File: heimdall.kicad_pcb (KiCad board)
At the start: 2 copper layers, 20 x 32 mm, 20 parts, among them P1 CONN, Q1 FDN304P, U1 ESP-01, U2 TLP222A, U3 TPS62177

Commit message: Various shuffling
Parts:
- R1: footprint Resistors_SMD:R_1206 -> Resistors_SMD:R_0603
- moved R2 8.41 mm to (102.2, 101.4)
- moved Q1 8.40 mm to (110.8, 101.3)
- moved R3 7.56 mm to (107.0, 103.1), turned to 0 degrees
- moved F1 5.67 mm to (109.1, 91.3), turned to 0 degrees
- moved C2 4.12 mm to (112.1, 102.0)
- moved C1 3.00 mm to (105.4, 95.3)
- moved L1 3.00 mm to (105.0, 98.5)
- moved U3 3.00 mm to (104.0, 94.4)
- moved C6 3.00 mm to (104.3, 93.1)
- moved D1 2.16 mm to (103.3, 87.0)
- moved R1 1.53 mm to (114.0, 102.7)
- moved C3 1.27 mm to (103.7, 107.2)
- moved C4 0.06 mm to (116.4, 108.4)
- moved C5 0.06 mm to (118.0, 108.4)
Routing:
- net +3V3: track 33.4 -> 26.6 mm
- net /SW0: track 11.1 -> 4.32 mm
- net /VCC: track 16.5 -> 11.5 mm
- net /PG: track 16.8 -> 11.8 mm
- net /PWROUT: track 4.48 -> 8.79 mm
- net /RELAY_TRIGGER: track 3.51 -> 4.77 mm
- net /SW0_IN: track 7.52 -> 8.53 mm
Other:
- board text added: "SW"
- board text removed: "SW0"
- board text removed: "SW1"

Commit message: More faffing
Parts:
- moved F2 3.14 mm to (117.2, 102.6)
- moved F1 2.05 mm to (110.9, 92.3), turned to 270 degrees
- moved C5 1.98 mm to (117.1, 106.6), turned to 0 degrees
- moved Q1 1.84 mm to (109.0, 101.3)
- moved R3 1.84 mm to (105.2, 103.1)
- moved C2 1.77 mm to (110.4, 102.4)
- moved C4 1.01 mm to (117.1, 109.2), turned to 0 degrees
- moved R1 0.97 mm to (113.1, 102.6)
- moved U2 0.25 mm to (114.6, 98.8)
- turned D3 to 180 degrees
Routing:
- net GND: track 26.5 -> 29.1 mm, vias 4 -> 5
- net Net-(C4-Pad1): track 14.0 -> 16.2 mm
- net /PG: track 11.8 -> 10.0 mm
- net +3V3: track 26.6 -> 25.0 mm
- net /PWROUT: track 8.79 -> 8.15 mm
- net /SW0_IN: track 8.53 -> 9.09 mm

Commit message: PMOS NMOS fun
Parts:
- Q1: value FDN304P -> FDN337N
- moved Q1 2.60 mm to (107.1, 103.1), turned to 0 degrees
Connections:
- Q1 pad 2: /PWROUT -> +3V3
- Q1 pad 3: +3V3 -> /PWROUT
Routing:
- net /PWROUT: track 8.15 -> 7.00 mm
- net +3V3: track 25.0 -> 25.8 mm
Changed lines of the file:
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@@
     (thickness 1.6)
     (drawings 15)
-    (tracks 136)
+    (tracks 135)
     (zones 0)
     (modules 20)
@@
   )
   (setup
-    (last_trace_width 0.5)
+    (last_trace_width 0.25)
     (user_trace_width 0.1)
     (user_trace_width 0.2)
@@
   )
   (module Housings_SSOT:SuperSOT-3 (layer F.Cu)
-    (at 108.966 101.2825 180)
-    (fp_text reference Q1 (at 1 1.1 180) (layer F.SilkS) hide
-      (effects (font (size 0.8 0.8) (thickness 0.15)))
-    )
-    (fp_text value FDN304P (at 1 -3.35 180) (layer F.Fab) hide
+    (at 107.1245 103.124)
+    (fp_text reference Q1 (at 1 1.1) (layer F.SilkS) hide
+      (effects (font (size 0.8 0.8) (thickness 0.15)))
+    )
+    (fp_text value FDN337N (at 1 -3.35) (layer F.Fab) hide
       (effects (font (size 0.8 0.8) (thickness 0.15)))
     )
@@
     (fp_line (start -0.51 -1.845) (end 2.41 -1.845) (layer F.SilkS) (width 0.15))
     (fp_line (start -0.51 -0.445) (end 2.41 -0.445) (layer F.SilkS) (width 0.15))
-    (pad 2 smd rect (at 0.95 -2.29 180) (size 0.76 0.76) (layers F.Cu F.Paste F.Mask)
+    (pad 2 smd rect (at 0.95 -2.29) (size 0.76 0.76) (layers F.Cu F.Paste F.Mask)
+      (net 2 +3V3))
+    (pad 3 smd rect (at 1.9 0) (size 0.76 0.76) (layers F.Cu F.Paste F.Mask)
       (net 9 /PWROUT))
-    (pad 3 smd rect (at 1.9 0 180) (size 0.76 0.76) (layers F.Cu F.Paste F.Mask)
-      (net 2 +3V3))
-    (pad 1 smd rect (at 0 0 180) (size 0.76 0.76) (layers F.Cu F.Paste F.Mask)
+    (pad 1 smd rect (at 0 0) (size 0.76 0.76) (layers F.Cu F.Paste F.Mask)
       (net 10 "Net-(C2-Pad2)"))
     (model ${KISYS3DMOD}/TO_SOT_Packages_SMD.3dshapes/SOT-23.wrl
@@
   (segment (start 106.96702 88.138) (end 107.643 88.81398) (width 0.5) (layer F.Cu) (net 1))
   (segment (start 107.482 87.62302) (end 106.96702 88.138) (width 0.5) (layer F.Cu) (net 1) (status 30))
-  (segment (start 106.553 96.03175) (end 107.066 96.54475) (width 0.25) (layer F.Cu) (net 2))
-  (segment (start 107.066 96.54475) (end 107.066 101.2825) (width 0.25) (layer F.Cu) (net 2))
-  (segment (start 102.1715 100.6595) (end 106.443 100.6595) (width 0.25) (layer F.Cu) (net 2))
-  (segment (start 106.443 100.6595) (end 107.066 101.2825) (width 0.25) (layer F.Cu) (net 2))
+  (segment (start 106.553 96.03175) (end 108.0745 97.55325) (width 0.25) (layer F.Cu) (net 2))
+  (segment (start 108.0745 97.55325) (end 108.0745 100.834) (width 0.25) (layer F.Cu) (net 2) (status 800000))
+  (segment (start 102.1715 100.6595) (end 107.9 100.6595) (width 0.25) (layer F.Cu) (net 2) (status C00000))
+  (segment (start 107.9 100.6595) (end 108.0745 100.834) (width 0.25) (layer F.Cu) (net 2) (status C00000))
   (segment (start 101.473 98.425) (end 101.473 100.5205) (width 0.25) (layer F.Cu) (net 2))
   (segment (start 103.04475 96.29275) (end 103.04475 96.85325) (width 0.25) (layer F.Cu) (net 2))
@@
   (segment (start 104.1908 96.29275) (end 104.04475 96.29275) (width 0.25) (layer F.Cu) (net 2))
   (segment (start 106.09725 98.45675) (end 106.09725 96.75075) (width 0.25) (layer F.Cu) (net 2))
-  (segment (start 110.96498 88.138) (end 110.871 88.23198) (width 0.5) (layer F.Cu) (net 3) (status C00000))
-  (segment (start 110.871 88.23198) (end 110.871 90.879) (width 0.5) (layer F.Cu) (net 3) (status C00000))
+  (segment (start 110.96498 88.138) (end 110.871 88.23198) (width 0.5) (layer F.Cu) (net 3))
+  (segment (start 110.871 88.23198) (end 110.871 90.879) (width 0.5) (layer F.Cu) (net 3))
   (segment (start 107.489 84.0105) (end 110.96498 87.48648) (width 0.5) (layer F.Cu) (net 3))
   (segment (start 110.96498 87.48648) (end 110.96498 88.138) (width 0.5) (layer F.Cu) (net 3))
@@
   (segment (start 111.3155 105.0805) (end 111.3155 106.6165) (width 0.25) (layer F.Cu) (net 6))
   (segment (start 111.5575 106.6165) (end 111.3155 106.6165) (width 0.25) (layer F.Cu) (net 6))
-  (segment (start 110.871 93.779) (end 111.961 93.779) (width 0.5) (layer F.Cu) (net 7) (status 400000))
-  (segment (start 111.961 93.779) (end 114.554 91.186) (width 0.5) (layer F.Cu) (net 7) (status 800000))
+  (segment (start 110.871 93.779) (end 111.961 93.779) (width 0.5) (layer F.Cu) (net 7))
+  (segment (start 111.961 93.779) (end 114.554 91.186) (width 0.5) (layer F.Cu) (net 7))
   (segment (start 103.6955 107.938) (end 110.097 107.938) (width 0.25) (layer F.Cu) (net 8))
   (segment (start 110.097 107.938) (end 111.3155 109.1565) (width 0.25) (layer F.Cu) (net 8))
+  (segment (start 109.0245 103.124) (end 110.375 103.124) (width 0.25) (layer F.Cu) (net 9) (status C00000))
+  (segment (start 110.375 103.124) (end 110.4265 103.1755) (width 0.25) (layer F.Cu) (net 9) (status C00000))
   (segment (start 110.4265 103.1755) (end 110.986 102.616) (width 0.25) (layer F.Cu) (net 9))
   (segment (start 110.986 102.616) (end 115.771 102.616) (width 0.25) (layer F.Cu) (net 9))
-  (segment (start 108.016 103.5725) (end 108.413 103.1755) (width 0.25) (layer F.Cu) (net 9))
-  (segment (start 108.413 103.1755) (end 110.4265 103.1755) (width 0.25) (layer F.Cu) (net 9))
-  (segment (start 108.966 101.2825) (end 109.359 101.6755) (width 0.25) (layer F.Cu) (net 10))
-  (segment (start 109.359 101.6755) (end 110.4265 101.6755) (width 0.25) (layer F.Cu) (net 10))
-  (segment (start 105.906 103.0605) (end 107.188 103.0605) (width 0.25) (layer F.Cu) (net 10))
-  (segment (start 107.188 103.0605) (end 108.966 101.2825) (width 0.25) (layer F.Cu) (net 10))
+  (segment (start 105.906 103.0605) (end 107.061 103.0605) (width 0.25) (layer F.Cu) (net 10) (status C00000))
+  (segment (start 107.061 103.0605) (end 108.446 101.6755) (width 0.25) (layer F.Cu) (net 10) (status 400000))
+  (segment (start 108.446 101.6755) (end 110.4265 101.6755) (width 0.25) (layer F.Cu) (net 10) (status 800000))
   (segment (start 103.54475 96.29275) (end 103.54475 96.64865) (width 0.25) (layer F.Cu) (net 11))
   (segment (start 103.54475 96.64865) (end 103.89725 97.00115) (width 0.25) (layer F.Cu) (net 11))

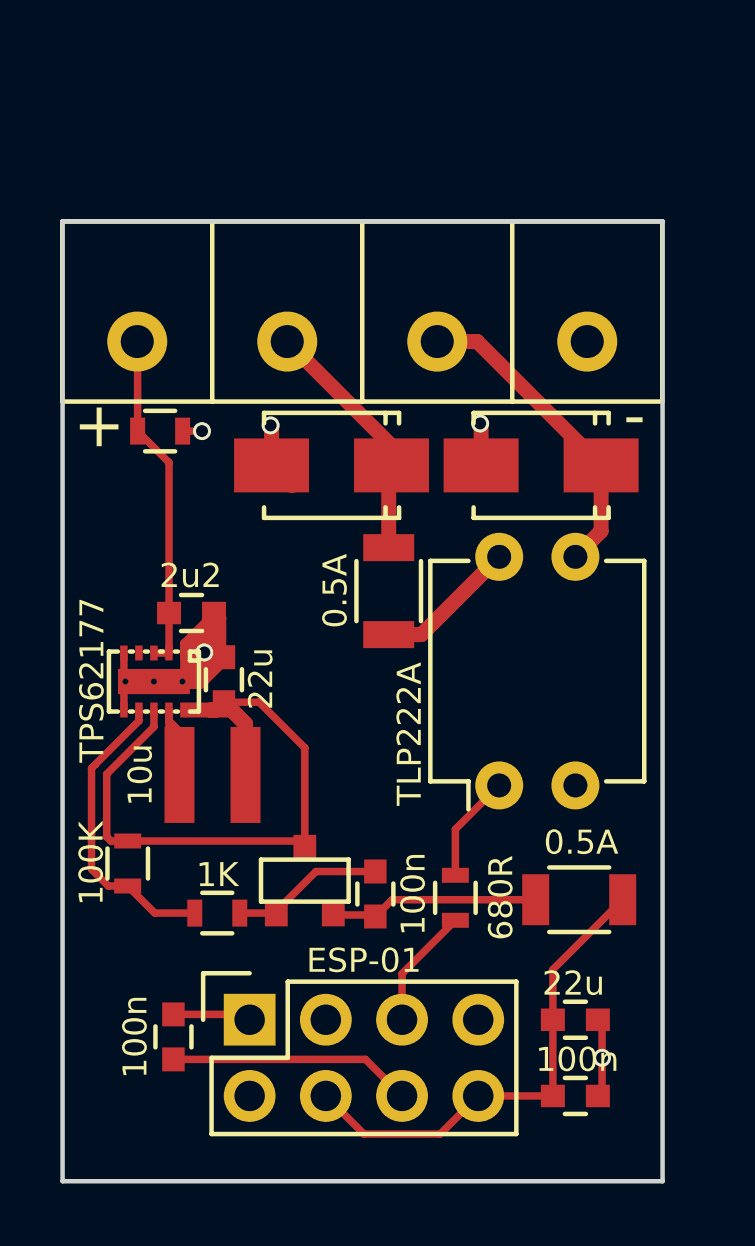
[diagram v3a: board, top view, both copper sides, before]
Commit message: Comments based on davids advice
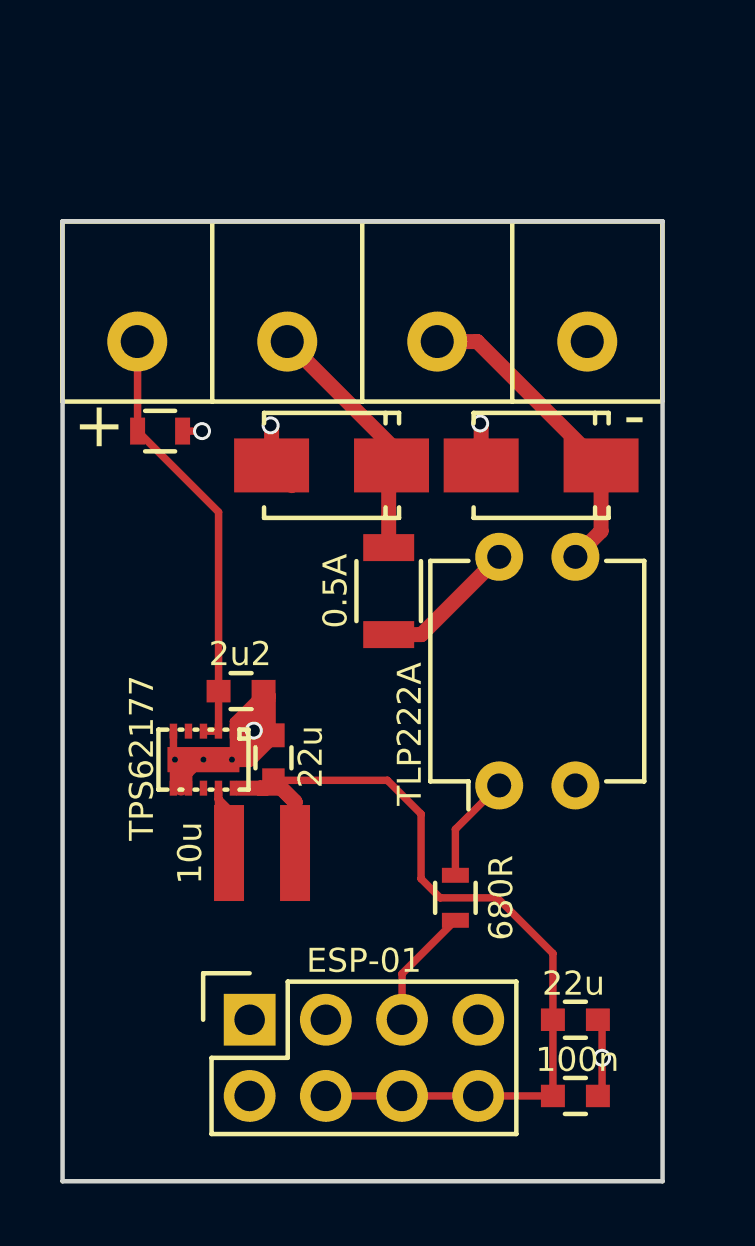
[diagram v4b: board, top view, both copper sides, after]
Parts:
- removed C2, C3: 100n, Capacitors_SMD:C_0603
- removed F2: 0.5A, Resistors_SMD:R_1206
- removed Q1: FDN337N, Housings_SSOT:SuperSOT-3
- removed R2: 100K, Resistors_SMD:R_0603
- removed R3: 1K, Resistors_SMD:R_0603
- moved C1 3.08 mm to (107.0, 97.9)
- moved L1 3.08 mm to (106.6, 101.1)
- moved U3 3.08 mm to (105.7, 97.0)
- moved C6 3.08 mm to (105.9, 95.7)
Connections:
- net /SW0_IN renamed Net-(D3-Pad1)
- net /VCC renamed /VIN
- C4 pad 1: Net-(C4-Pad1) -> +3V3
- C5 pad 1: Net-(C4-Pad1) -> +3V3
- U1 pad 4: Net-(C4-Pad1) -> +3V3
- U1 pad 6: Net-(C3-Pad1) -> +3V3
- U1 pad 8: Net-(C4-Pad1) -> +3V3
- U3 pad 7: /PG -> GND
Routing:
- net Net-(C4-Pad1): track 16.2 -> 0.00 mm
- net /PG: track 10.0 -> 0.00 mm
- net Net-(C3-Pad1): track 8.12 -> 0.00 mm
- net +3V3: track 25.8 -> 32.9 mm
- net /PWROUT: track 7.00 -> 0.00 mm
- net Net-(C2-Pad2): track 5.09 -> 0.00 mm
- net /VIN: track 11.5 -> 14.8 mm
- net GND: track 29.1 -> 31.0 mm
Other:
- rule pad_to_mask_clearance: 0.2 -> 0

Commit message: Missing track
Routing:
- net +3V3: track 32.9 -> 45.0 mm
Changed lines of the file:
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@@
   (general
     (links 37)
-    (no_connects 1)
+    (no_connects 0)
     (area 99.924999 79.924999 120.075001 112.075001)
     (thickness 1.6)
     (drawings 15)
-    (tracks 118)
+    (tracks 124)
     (zones 0)
     (modules 14)
@@
   (segment (start 106.96702 88.138) (end 107.643 88.81398) (width 0.5) (layer F.Cu) (net 1))
   (segment (start 107.482 87.62302) (end 106.96702 88.138) (width 0.5) (layer F.Cu) (net 1) (status 30))
-  (segment (start 111.3155 109.1565) (end 108.7755 109.1565) (width 0.25) (layer F.Cu) (net 2) (status C00000))
-  (segment (start 113.8555 109.1565) (end 111.3155 109.1565) (width 0.25) (layer F.Cu) (net 2) (status C00000))
-  (segment (start 107.02925 98.63525) (end 110.82725 98.63525) (width 0.25) (layer F.Cu) (net 2))
+  (segment (start 104.69575 98.89625) (end 104.69575 102.79075) (width 0.25) (layer F.Cu) (net 2) (status 400000))
+  (segment (start 108.585 102.8065) (end 108.585 98.63525) (width 0.25) (layer F.Cu) (net 2))
+  (segment (start 108.3945 102.997) (end 108.585 102.8065) (width 0.25) (layer F.Cu) (net 2))
+  (segment (start 104.902 102.997) (end 108.3945 102.997) (width 0.25) (layer F.Cu) (net 2))
+  (segment (start 104.69575 102.79075) (end 104.902 102.997) (width 0.25) (layer F.Cu) (net 2))
+  (segment (start 111.3155 109.1565) (end 108.7755 109.1565) (width 0.25) (layer F.Cu) (net 2))
+  (segment (start 113.8555 109.1565) (end 111.3155 109.1565) (width 0.25) (layer F.Cu) (net 2))
+  (segment (start 107.02925 98.63525) (end 108.585 98.63525) (width 0.25) (layer F.Cu) (net 2))
+  (segment (start 108.585 98.63525) (end 110.82725 98.63525) (width 0.25) (layer F.Cu) (net 2))
   (segment (start 116.344 104.406) (end 116.344 106.6165) (width 0.25) (layer F.Cu) (net 2))
   (segment (start 114.4905 102.5525) (end 116.344 104.406) (width 0.25) (layer F.Cu) (net 2))

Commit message: Minor shuffling and finishing up.
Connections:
- U1 pad 2: (no net) -> Net-(U1-Pad2)
- U1 pad 3: (no net) -> Net-(U1-Pad3)
- U1 pad 7: (no net) -> Net-(U1-Pad7)
- U3 pad 4: (no net) -> GND
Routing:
- net GND: track 31.0 -> 29.1 mm
- net +3V3: track 45.0 -> 43.8 mm
- net Net-(D3-Pad1): track 9.09 -> 9.87 mm
- net /VIN: track 14.8 -> 15.4 mm

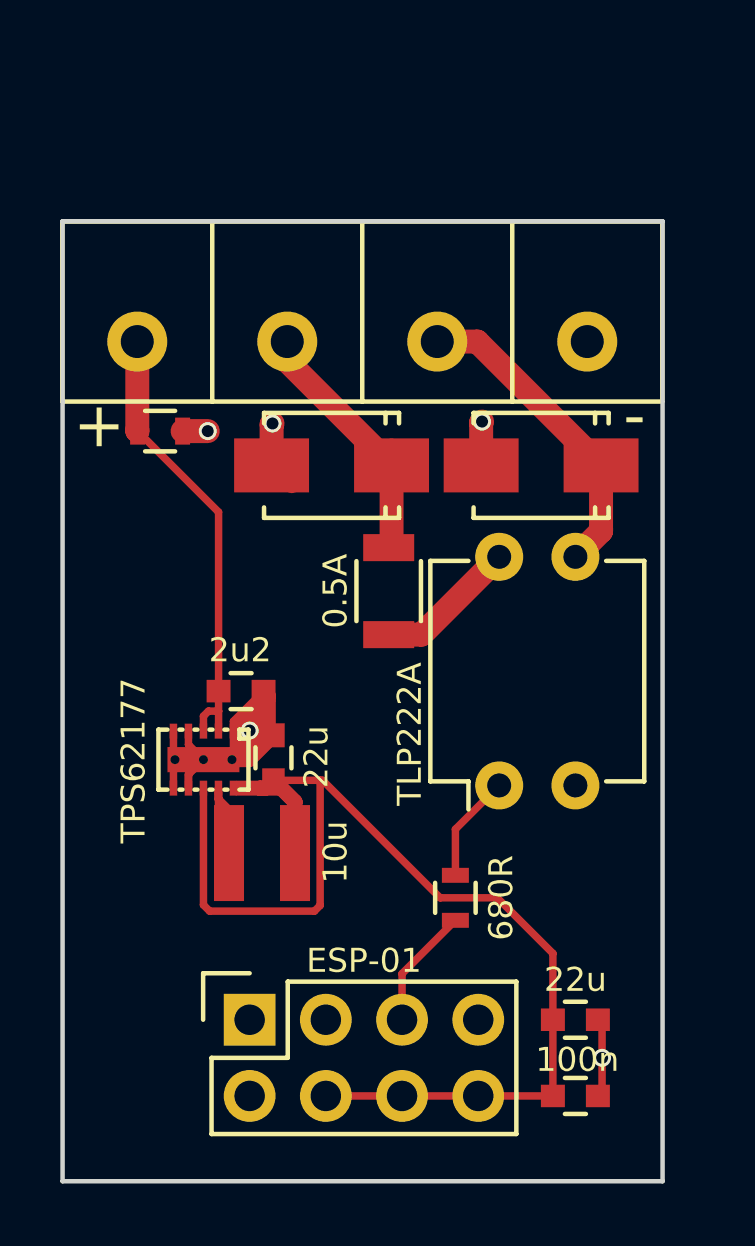
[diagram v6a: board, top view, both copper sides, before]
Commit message: Various shuffling
* Switched to agg footprints where possible
* Farnell numbers and data sheets
* Status LEDs for dev
* Schematic shuffling
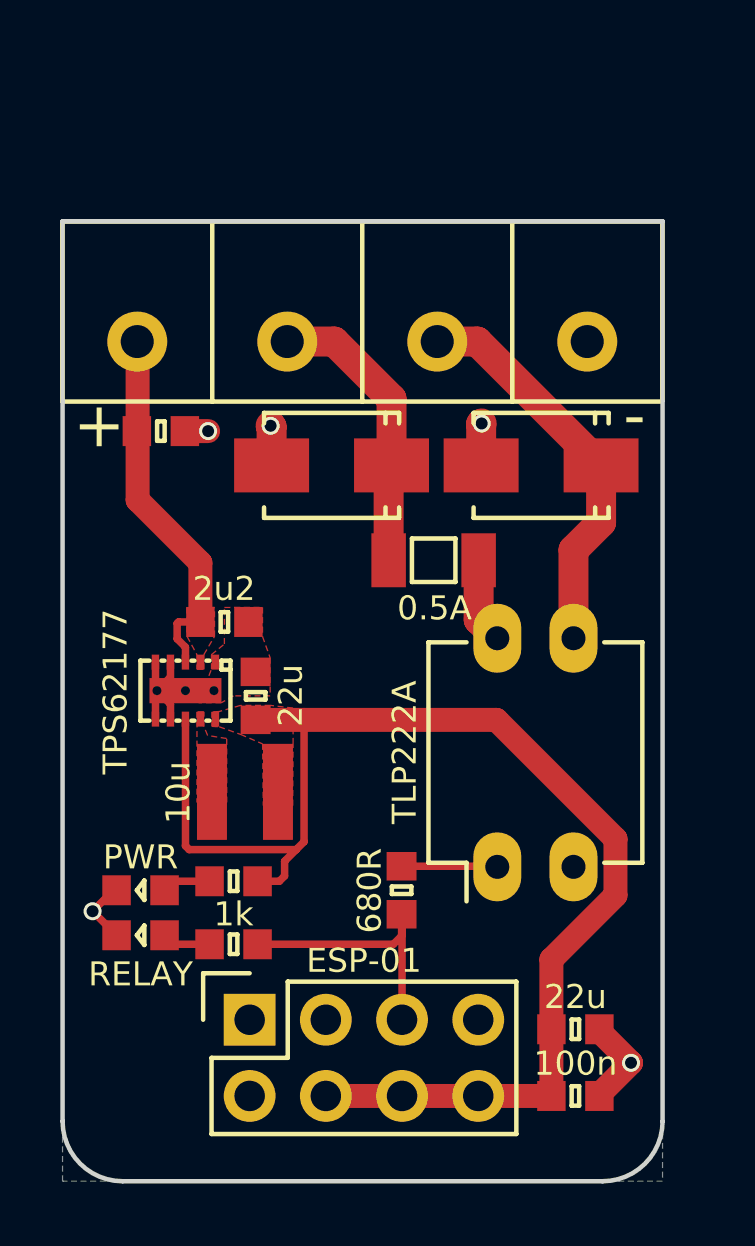
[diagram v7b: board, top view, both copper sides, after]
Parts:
- added D2: PWR, agg:0603-LED, F.Cu at (102.6, 102.3)
- added D5: RELAY, agg:0603-LED, F.Cu at (102.6, 103.8)
- added R2: 1k, agg:0603, F.Cu at (105.7, 102.0)
- added R3: 1k, agg:0603, F.Cu at (105.7, 104.1)
- C1, C4, C5, C6: footprint Capacitors_SMD:C_0603 -> agg:0603
- D1, R1: footprint Resistors_SMD:R_0603 -> agg:0603
- F1: footprint Resistors_SMD:R_1206 -> agg:1206
- U2: footprint Housings_DIP:DIP-4_W7.62mm -> Housings_DIP:DIP-4_W7.62mm_LongPads
- moved U2 2.71 mm to (114.5, 101.5)
- moved U3 2.38 mm to (105.1, 94.7)
- moved C6 2.37 mm to (105.4, 93.4)
- moved C1 2.15 mm to (106.4, 95.8)
- moved L1 2.12 mm to (106.1, 99.0)
- moved F1 1.82 mm to (112.4, 91.3), turned to 0 degrees
- moved R1 1.81 mm to (111.3, 102.3)
- moved C5 0.32 mm to (117.1, 106.9)
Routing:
- net GND: track 29.1 -> 13.5 mm
- net Net-(L1-Pad1): track 6.93 -> 0.00 mm
- net /RELAY_TRIGGER: track 4.29 -> 9.18 mm
- net /VIN: track 15.4 -> 12.7 mm
- net /SW1: track 10.6 -> 13.3 mm
- net /SW0: track 4.76 -> 2.79 mm
- net Net-(D5-Pad2): track 0.00 -> 1.62 mm
- net Net-(D2-Pad2): track 0.00 -> 1.62 mm
- net +3V3: track 43.8 -> 45.1 mm
- net Net-(R1-Pad1): track 3.92 -> 3.20 mm
- net Net-(D3-Pad1): track 9.87 -> 10.4 mm
- added copper zone on F.Cu, net +3V3
- added copper zone on F.Cu, net /VIN
- added copper zone on F.Cu, net GND
- added copper zone on F.Cu, net Net-(L1-Pad1)
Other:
- outline, holes or cut-outs redrawn
- board text added: "Hark <pcb@harkonen.net> Heimdall V1 26/06/16 http://github.com/HarkonenBade/heimdall"
- board text removed: "Hark <pcb@harkonen.net> Heimdall V1 08/06/16 http://github.com/HarkonenBade/heimdall"

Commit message: Various
* changed TVS diodes over to new agg:SMA
* Swapped terminal block for one from HL
* Setup for board panelizing
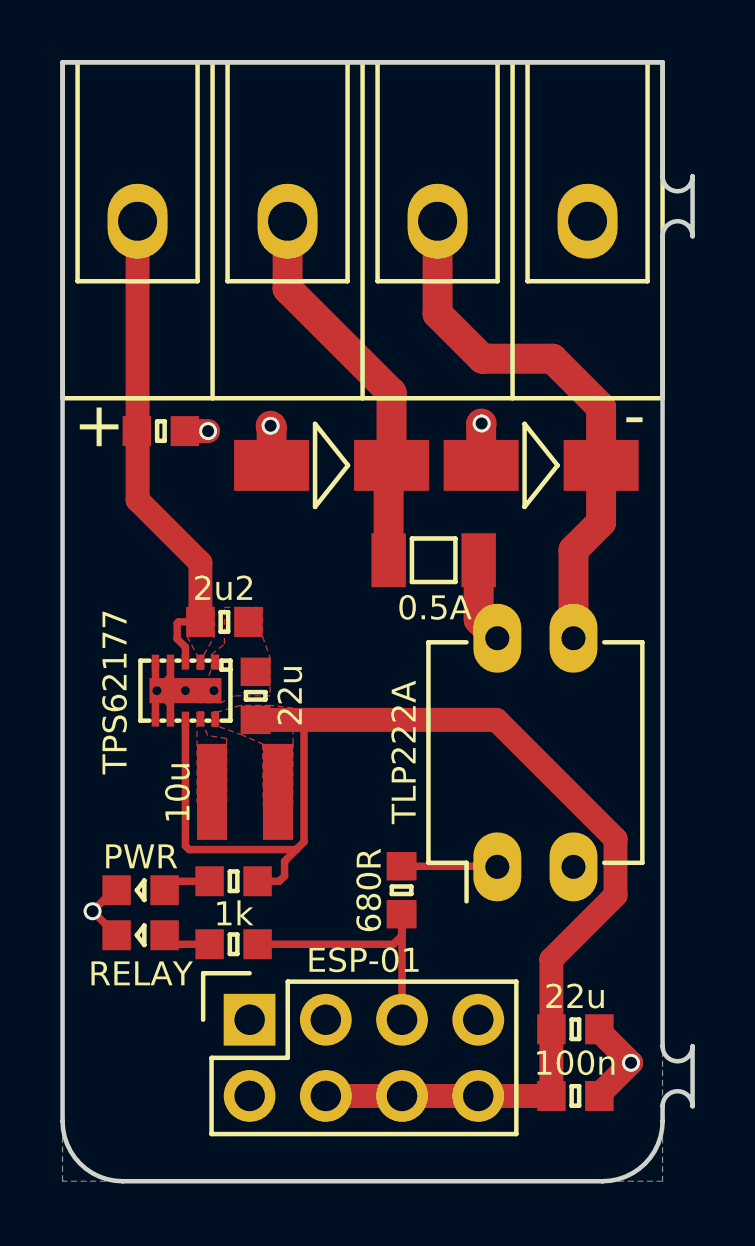
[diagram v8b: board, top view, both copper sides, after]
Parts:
- D3, D4: footprint Diodes_SMD:SMA_Standard -> agg:DO-214AC-SMA
- P1: footprint footprints:CTB1500-4 -> footprints:MKDS-4
- moved P1 4.01 mm to (102.5, 80.0)
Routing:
- net /SW1: track 13.3 -> 17.9 mm
- net /VIN: track 12.7 -> 16.5 mm
- net Net-(D3-Pad1): track 10.4 -> 12.8 mm
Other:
- board size 20 x 32 mm -> 21 x 37.3 mm
